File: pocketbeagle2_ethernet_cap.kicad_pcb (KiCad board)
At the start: 4 copper layers, 35.3 x 55.3 mm, 84 parts, among them J1 RJ45_1840888-1, J2 Header_18x02_2.54mm_2.54mm_St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, J3 Header_18x02_2.54mm_2.54mm_St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, Q1 BSS138LT1G, Q2 BSS138LT1G, Q3 BSS138LT1G, U1 PocketBeagle2, U2 DP83867IRPAPR, U3 TPS7A2011PDBVR, U4 TPS7A2025PDBVR, Y1 25M

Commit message: Clear P1/P2 headers: move R13, R9, U3; re-route TD1
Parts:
- C37, C38, R31, R32: moved to B.Cu
- moved C37 209.2 mm to (199.2, 81.2)
- moved R31 205.6 mm to (190.5, 91.6)
- moved R32 201.4 mm to (190.0, 89.9), turned to 90 degrees
- moved C38 201.2 mm to (193.5, 81.0), turned to -90 degrees
- moved R9 23.8 mm to (204.5, 73.9), turned to 180 degrees
- moved U3 1.65 mm to (204.2, 76.3)
- moved R13 0.25 mm to (187.4, 62.6)
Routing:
- net /RGMII_TD1_CPU_to_PHY: track 2.15 -> 27.5 mm
- net Net-(U2-TX_D1): track 46.8 -> 21.6 mm
- net /VDD_1V1: track 47.4 -> 55.8 mm
- net GND: track 46.7 -> 53.8 mm
- net /network/phy/LED0_PHY_to_Q1: track 57.4 -> 59.5 mm, vias 1 -> 2
- net /VDD_3V3: track 176.7 -> 178.7 mm

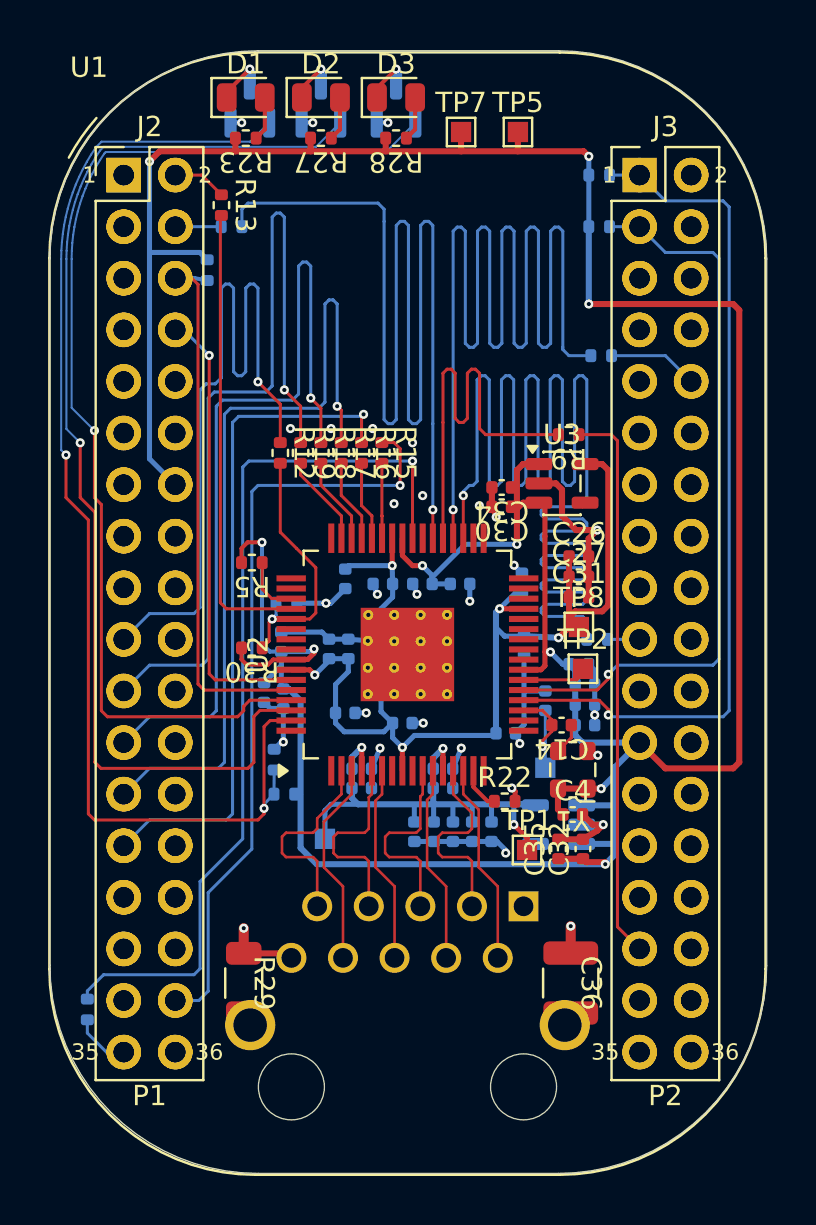
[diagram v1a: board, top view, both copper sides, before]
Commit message: Add GND/chassis pours on F/B and stitching via fence
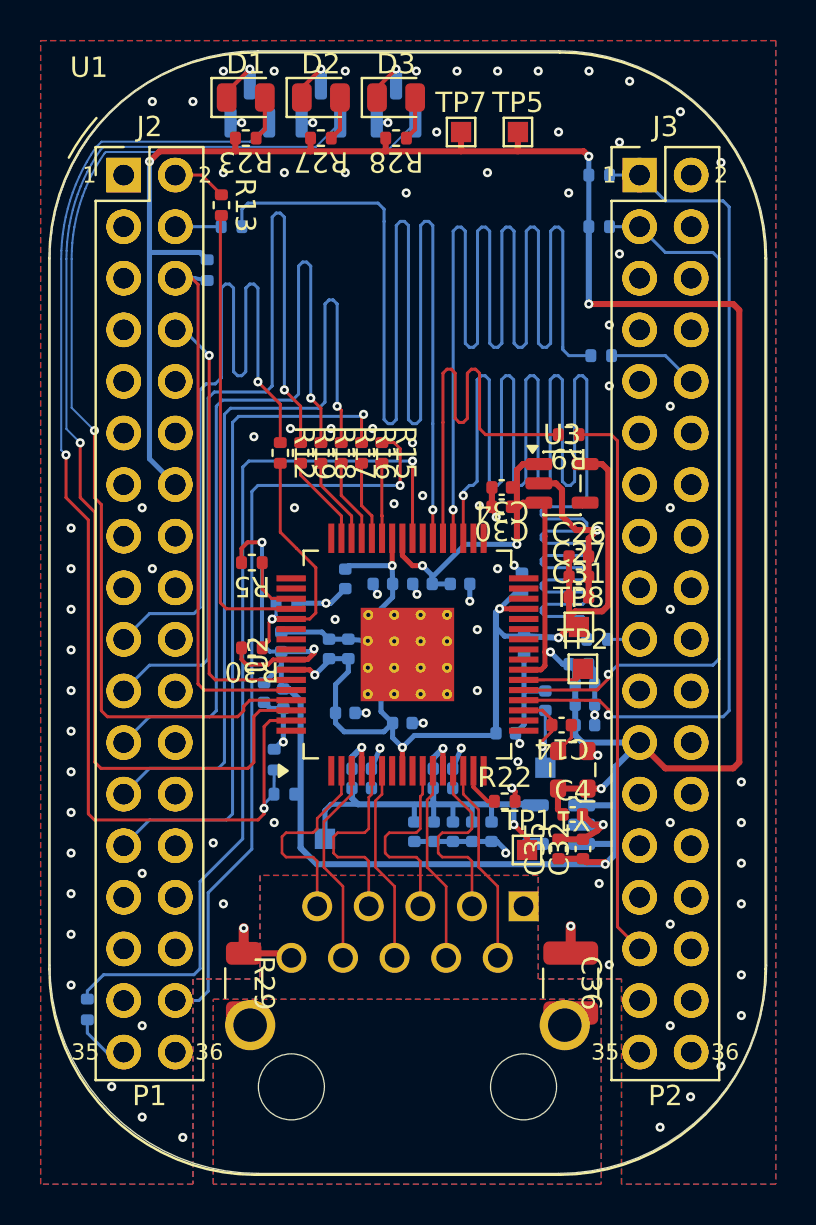
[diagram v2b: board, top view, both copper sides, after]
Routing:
- net GND: vias 30 -> 101
- added copper zone on B.Cu, net /network/rj45_connector_port0/CHASSIS
- added copper zone on F.Cu, net /network/rj45_connector_port0/CHASSIS
- added copper zone on B.Cu, net GND
- added copper zone on F.Cu, net GND
